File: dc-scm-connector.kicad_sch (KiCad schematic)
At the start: 57 parts, among them J701 PCB-Edge_DC-SCM-2.1_2x84_Rev-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, U701 TXS0102DQER

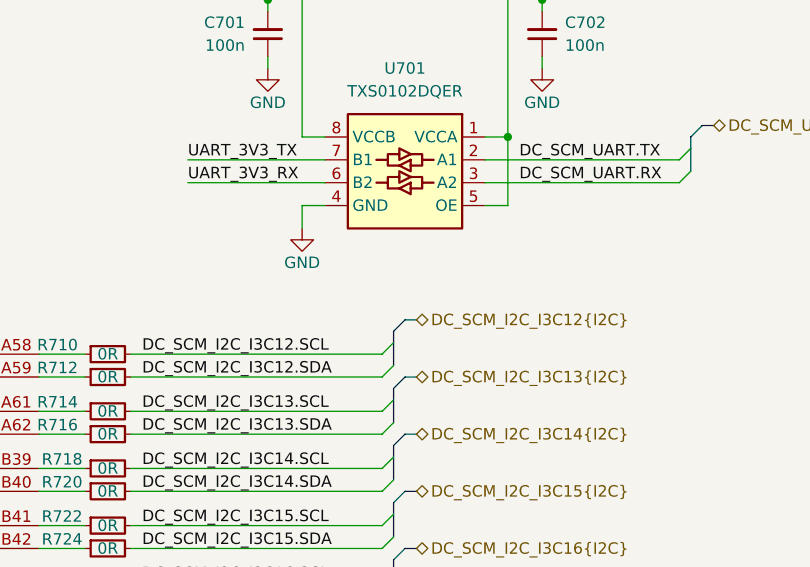
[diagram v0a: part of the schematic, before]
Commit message: [#100501] Add optional pullup for PECI address pin, add note about its address and translator having internal pullups
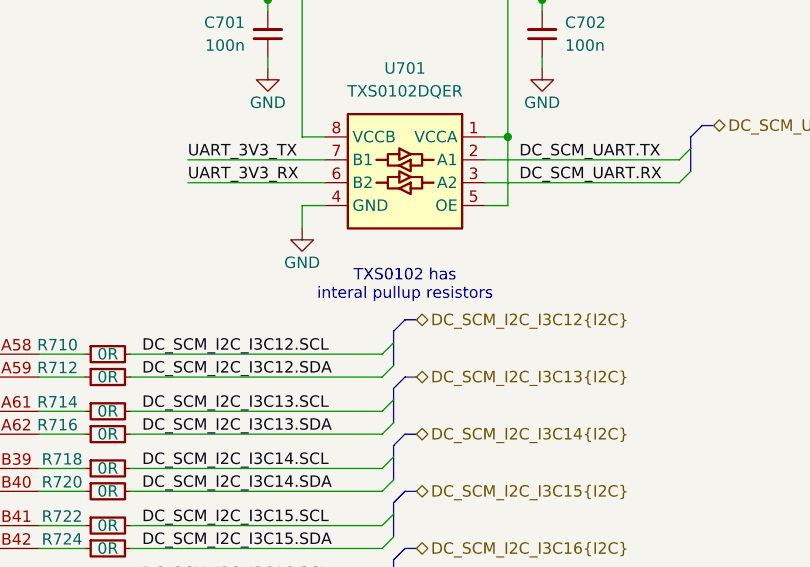
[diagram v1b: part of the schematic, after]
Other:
- note added: "TXS0102 has interal pullup resistors"
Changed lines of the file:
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@@
+		)
+	)
+	(text "TXS0102 has\ninteral pullup resistors"
+		(exclude_from_sim no)
+		(at 189.23 119.38 0)
+		(effects
+			(font
+				(size 1.27 1.27)
+			)
 		)
 	)

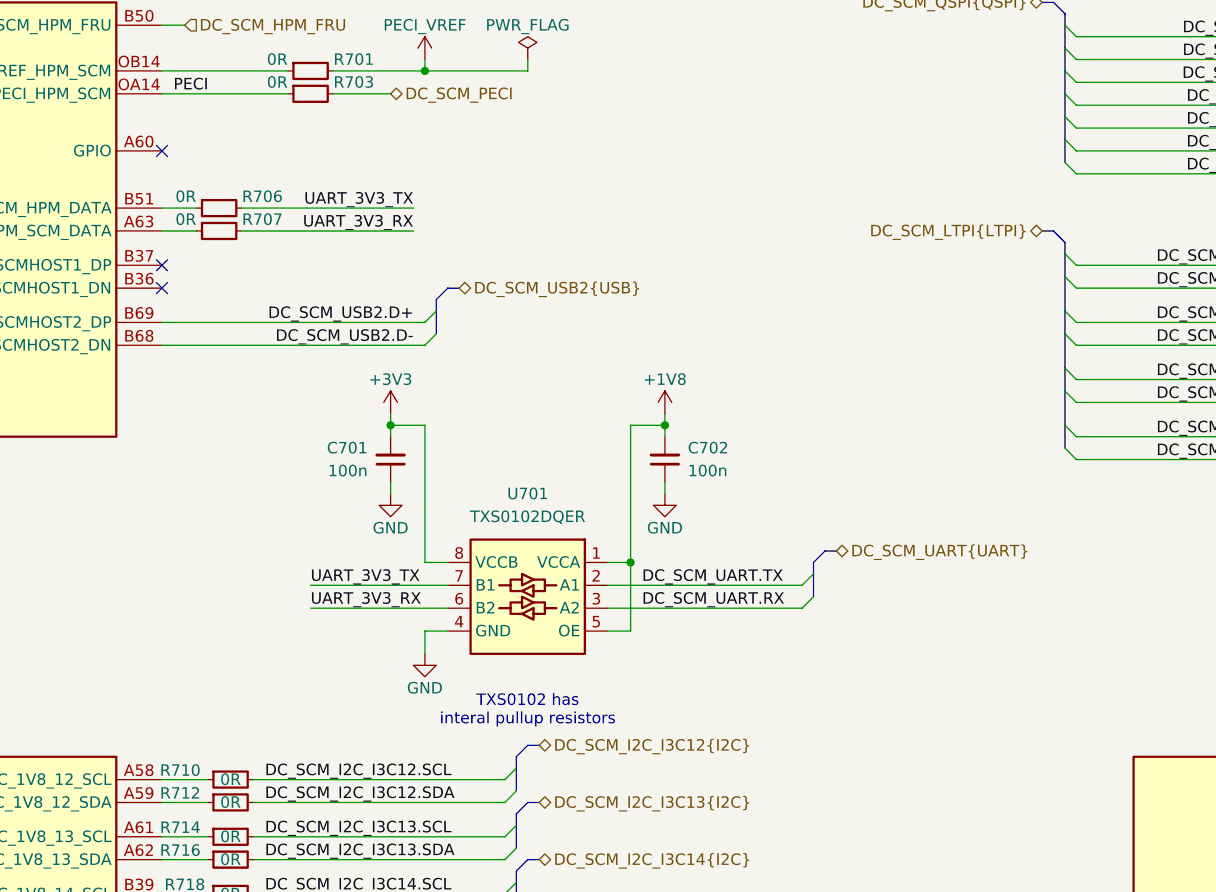
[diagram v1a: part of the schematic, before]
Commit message: [#100501] Move UART level shifter from DC-SCM to HVIO schematic sheet
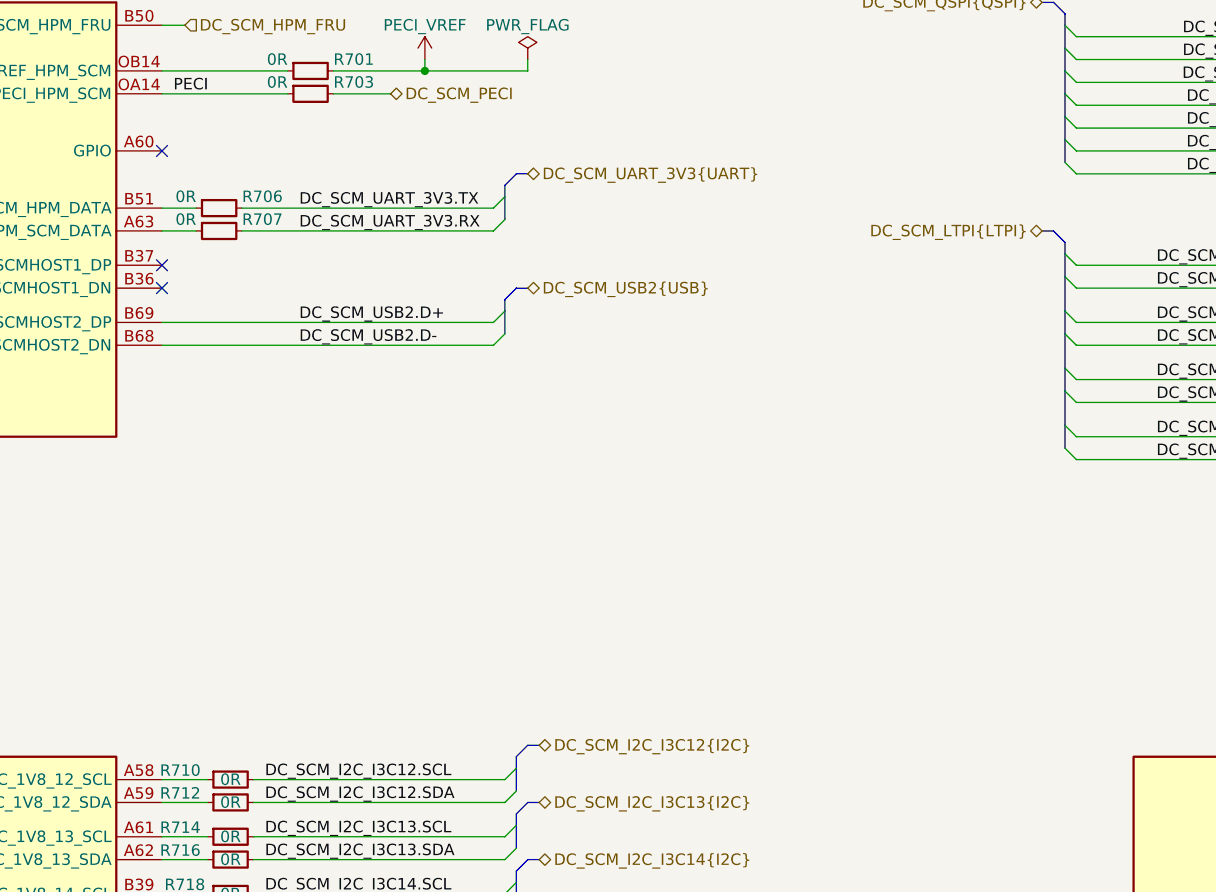
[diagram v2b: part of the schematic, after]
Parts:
- removed C701, C702: C_100n_0402, antmicro-footprints:C_0402_1005Metric, symbol antmicroCapacitors0402:C_100n_0402
- removed U701: TXS0102DQER, antmicro-footprints:X2SON8_1.4x1x0.32mm_P0.35mm, symbol antmicroLogicTranslatorsLevelShifters:TXS0102DQER
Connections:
- net UART_3V3_RX renamed DC_SCM_UART_3V3.RX
- net UART_3V3_TX renamed DC_SCM_UART_3V3.TX
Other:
- note removed: "TXS0102 has interal pullup resistors"

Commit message: [#100282] Add missing schematic sheet names and align them all
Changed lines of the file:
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@@
 	(text "DC-SCM 2.1 connector"
 		(exclude_from_sim no)
-		(at 222.25 24.13 0)
+		(at 210.82 25.4 0)
 		(effects
 			(font

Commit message: [#100501] Reannotate schematic
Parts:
- renumbered J701 to J3, R701 to R20, R702 to R21, R703 to R22, R704 to R23, R705 to R24, R706 to R25, R707 to R26, R708 to R27, R709 to R28, R710 to R29, R711 to R30, R712 to R31, R713 to R32, R714 to R33, R715 to R34, R716 to R35, R717 to R36, R718 to R37, R719 to R38, R720 to R39, R721 to R40, R722 to R41, R723 to R42, R724 to R43, R725 to R44, R726 to R45, R727 to R46, R728 to R47, R729 to R48, R730 to R49, R731 to R50, R732 to R51, R733 to R52, R734 to R53, R735 to R54, R736 to R55, R737 to R56, R738 to R57, R739 to R58, R740 to R59, R741 to R60, R742 to R61, R743 to R62, R744 to R63, R745 to R64, R746 to R65, R747 to R66, R748 to R67, R749 to R68, R750 to R69, R751 to R70, R752 to R71, R753 to R72

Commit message: [#100501] Add 0Rs to DC-SCM QSPI, eSPI, NC-SI, JTAG  and USB
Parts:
- added R20, R21, R22, R23, R25, R26, R29, R30, R32, R33, R35, R36, R37, R38, R39, R40, R41, R43, R45, R46, R47, R48, R49, R50, R52, R53, R54, R55, R56: R_0R_0402, antmicro-footprints:R_0402_1005Metric, symbol antmicroResistors0402:R_0R_0402
- renumbered R20 to R24, R21 to R27, R22 to R28, R23 to R31, R44 to R320, R45 to R321, R46 to R322, R47 to R323, R48 to R324, R49 to R325, R50 to R326, R51 to R327, R52 to R328, R53 to R329, R54 to R330, R55 to R331, R56 to R332, R57 to R333, R58 to R334, R59 to R335, R60 to R336, R61 to R337, R62 to R338, R63 to R339, R24 to R34, R64 to R340, R65 to R341, R66 to R342, R67 to R343, R68 to R344, R69 to R345, R70 to R346, R71 to R347, R72 to R348, R25 to R42, R26 to R44, R27 to R51, R28 to R57, R29 to R58, R30 to R59, R31 to R60, R32 to R61, R33 to R62, R34 to R63, R35 to R64, R36 to R65, R37 to R66, R38 to R67, R39 to R68, R40 to R69, R41 to R70, R42 to R71, R43 to R72
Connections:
- net DC_SCM_ESPI.IO0: now also R30.1; no longer J3.B4 (ESPI_HPMCNTRL_IO_0)
- net DC_SCM_ESPI.IO1: now also R33.1; no longer J3.B5 (ESPI_HPMCNTRL_IO_1)
- net DC_SCM_ESPI.IO2: now also R36.1; no longer J3.B6 (ESPI_HPMCNTRL_IO_2)
- net DC_SCM_ESPI.IO3: now also R38.1; no longer J3.B7 (ESPI_HPMCNTRL_IO_3)
- net DC_SCM_ESPI.SCK: now also R21.1; no longer J3.B1 (ESPI_HPMCNTRL_CLK)
- net DC_SCM_ESPI.~{ALERT0}: now also R40.1; no longer J3.B8 (ESPI_HPMCNTRL_ALERT0_N)
- net DC_SCM_ESPI.~{CS0}: now also R23.1; no longer J3.B2 (ESPI_HPMCNTRL_CS0_N)
- net DC_SCM_ESPI.~{RESET}: now also R26.1; no longer J3.B3 (ESPI_HPMCNTRL_RESET_N)
- net DC_SCM_JTAG.TCK: now also R39.1; no longer J3.A8 (JTAG_SCMCNTRL_TCK)
- net DC_SCM_JTAG.TDI: now also R43.1; no longer J3.A10 (JTAG_SCMCNTRL_TDI)
- net DC_SCM_JTAG.TDO: now also R41.1; no longer J3.A9 (JTAG_SCMCNTRL_TDO)
- net DC_SCM_JTAG.TMS: now also R45.1; no longer J3.A11 (JTAG_SCMCNTRL_TMS)
- net DC_SCM_JTAG.TRST: now also R46.1; no longer J3.A12 (JTAG_SCMCNTRL_TRST_N)
- net DC_SCM_NC-SI.CRS_DV: now also R50.1; no longer J3.B44 (NCSI_HPM_SCM_CRS_DV)
- net DC_SCM_NC-SI.REF_CLK: now also R48.1; no longer J3.B43 (NCSI_HPM_SCM_CLK)
- net DC_SCM_NC-SI.RXD0: now also R52.1; no longer J3.B48 (NCSI_HPM_SCM_D0)
- net DC_SCM_NC-SI.RXD1: now also R53.1; no longer J3.B49 (NCSI_HPM_SCM_D1)
- net DC_SCM_NC-SI.TXD0: now also R55.1; no longer J3.B46 (NCSI_SCM_HPM_D0)
- net DC_SCM_NC-SI.TXD1: now also R56.1; no longer J3.B47 (NCSI_SCM_HPM_D1)
- net DC_SCM_NC-SI.TX_EN: now also R54.1; no longer J3.B45 (NCSI_SCM_HPM_TX_EN)
- net DC_SCM_QSPI.IO0: now also R29.1; no longer J3.B14 (QSPI_HPMCNTRL_IO_0)
- net DC_SCM_QSPI.IO1: now also R32.1; no longer J3.B15 (QSPI_HPMCNTRL_IO_1)
- net DC_SCM_QSPI.IO2: now also R35.1; no longer J3.B16 (QSPI_HPMCNTRL_IO_2)
- net DC_SCM_QSPI.IO3: now also R37.1; no longer J3.B17 (QSPI_HPMCNTRL_IO_3)
- net DC_SCM_QSPI.SCK: now also R25.1; no longer J3.B12 (QSPI_HPMCNTRL_CLK)
- net DC_SCM_QSPI.~{CS0}: now also R20.1; no longer J3.B13 (QSPI_HPMCNTRL_CS0_N)
- net DC_SCM_QSPI.~{CS1}: now also R22.1; no longer J3.B18 (QSPI_HPMCNTRL_CS1_N)
- net DC_SCM_USB2.D+: now also R47.2; no longer J3.B69 (USB2_SCMHOST2_DP)
- net DC_SCM_USB2.D-: now also R49.2; no longer J3.B68 (USB2_SCMHOST2_DN)
- new net: J3.A9 (JTAG_SCMCNTRL_TDO), R41.2
- new net: J3.B12 (QSPI_HPMCNTRL_CLK), R25.2
- new net: J3.B49 (NCSI_HPM_SCM_D1), R53.2
- new net: J3.B2 (ESPI_HPMCNTRL_CS0_N), R23.2
- new net: J3.A8 (JTAG_SCMCNTRL_TCK), R39.2
- new net: J3.B13 (QSPI_HPMCNTRL_CS0_N), R20.2
- new net: J3.B44 (NCSI_HPM_SCM_CRS_DV), R50.2
- new net: J3.B15 (QSPI_HPMCNTRL_IO_1), R32.2
- new net: J3.B5 (ESPI_HPMCNTRL_IO_1), R33.2
- new net: J3.B68 (USB2_SCMHOST2_DN), R49.1
- new net: J3.B48 (NCSI_HPM_SCM_D0), R52.2
- new net: J3.A10 (JTAG_SCMCNTRL_TDI), R43.2
- new net: J3.A11 (JTAG_SCMCNTRL_TMS), R45.2
- new net: J3.A12 (JTAG_SCMCNTRL_TRST_N), R46.2
- new net: J3.B69 (USB2_SCMHOST2_DP), R47.1
- new net: J3.B1 (ESPI_HPMCNTRL_CLK), R21.2
- new net: J3.B14 (QSPI_HPMCNTRL_IO_0), R29.2
- new net: J3.B16 (QSPI_HPMCNTRL_IO_2), R35.2
- new net: J3.B17 (QSPI_HPMCNTRL_IO_3), R37.2
- new net: J3.B18 (QSPI_HPMCNTRL_CS1_N), R22.2
- new net: J3.B3 (ESPI_HPMCNTRL_RESET_N), R26.2
- new net: J3.B4 (ESPI_HPMCNTRL_IO_0), R30.2
- new net: J3.B43 (NCSI_HPM_SCM_CLK), R48.2
- new net: J3.B45 (NCSI_SCM_HPM_TX_EN), R54.2
- new net: J3.B46 (NCSI_SCM_HPM_D0), R55.2
- new net: J3.B47 (NCSI_SCM_HPM_D1), R56.2
- new net: J3.B6 (ESPI_HPMCNTRL_IO_2), R36.2
- new net: J3.B7 (ESPI_HPMCNTRL_IO_3), R38.2
- new net: J3.B8 (ESPI_HPMCNTRL_ALERT0_N), R40.2
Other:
- moved on the sheet: J3C, R27, R31, R34

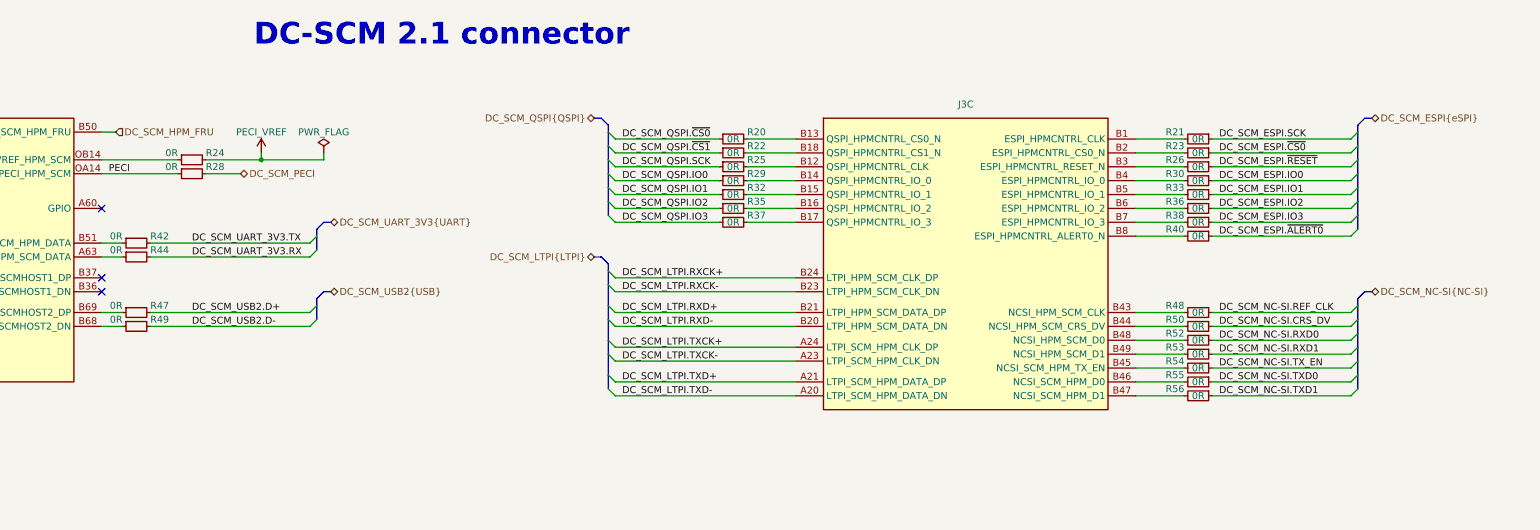
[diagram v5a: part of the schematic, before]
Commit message: [#100501] Add Tag-Connect to JTAG and config EEPROM to FTDI, connect DC-SCM USB1 to USB controller
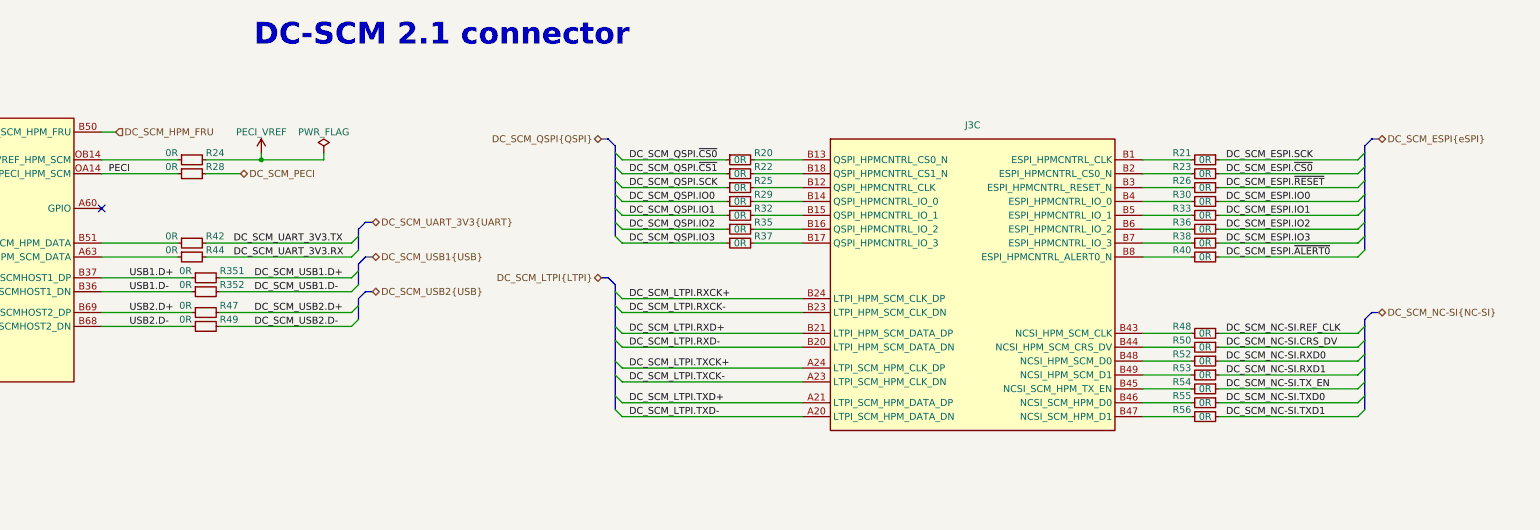
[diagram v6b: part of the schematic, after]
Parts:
- added R351, R352: R_0R_0402, antmicro-footprints:R_0402_1005Metric, symbol antmicroResistors0402:R_0R_0402
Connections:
- net USB2.D-: now reaches J3.B68 (USB2_SCMHOST2_DN), R49.1
- net USB1.D-: now reaches J3.B36 (USB2_SCMHOST1_DN)
- net USB1.D-: now also R352.1
- net USB1.D+: now reaches J3.B37 (USB2_SCMHOST1_DP)
- net USB1.D+: now also R351.1
- net USB2.D+: now reaches J3.B69 (USB2_SCMHOST2_DP), R47.1
- new net DC_SCM_USB1.D+: R351.2
- new net DC_SCM_USB1.D-: R352.2
- no-connect marks 21 -> 19
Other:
- moved on the sheet: J3C, R20, R21, R22, R23, R25, R26, R29, R30, R32, R33, R35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
